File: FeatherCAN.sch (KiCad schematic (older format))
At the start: 29 parts, among them J1 Feather Long, J2 Feather Short, J3 Header, J4 PicoBlade, U1 DS3231MZ, U2 MCP2515-xST, U3 MCP2551-I-SN, U4 5V, Y1 16MHz

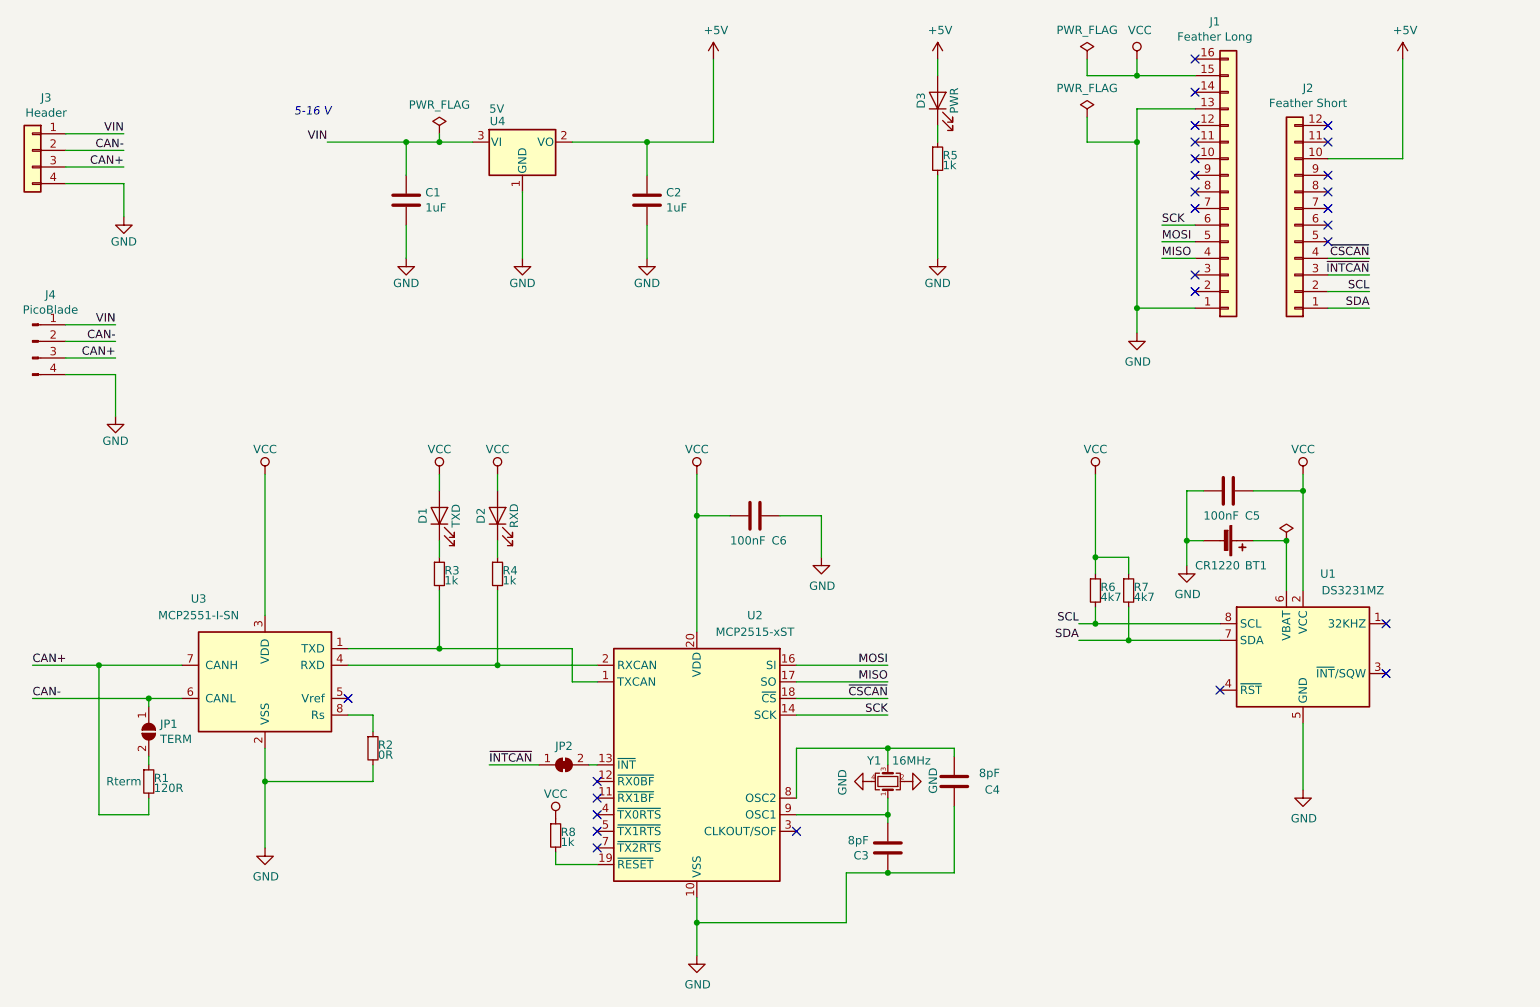
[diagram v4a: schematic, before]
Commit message: add CAN transeiver lines for STM32 Feather peripheral
STM32 Feather has CAN RX/TX on #9 and #10. Can be cut if user wants to
use pins on other Feather.
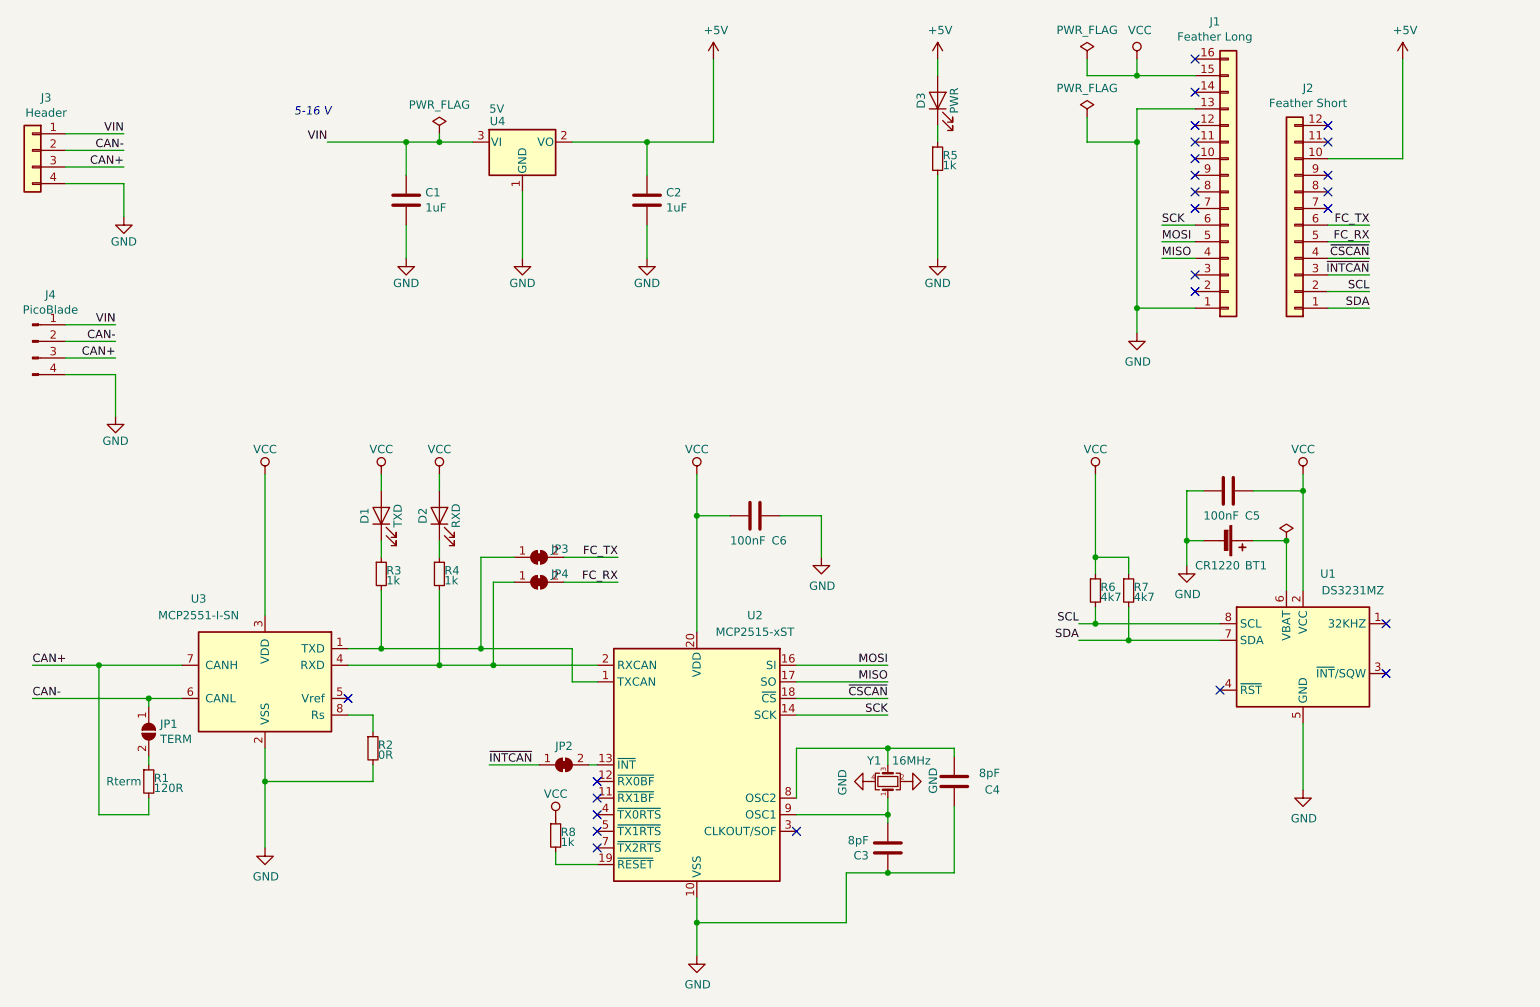
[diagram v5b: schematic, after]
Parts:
- added JP3, JP4: INT, KiCad/Jumper.pretty:SolderJumper-2_P1.3mm_Bridged_RoundedPad1.0x1.5mm, symbol Jumper:SolderJumper_2_Bridged
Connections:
- net FC_RX: now reaches J2.5 (Pin_5)
- net FC_RX: now also JP4.2 (B)
- net FC_TX: now reaches J2.6 (Pin_6)
- net FC_TX: now also JP3.2 (B)
- net at R3.2, U2.1 (TXCAN), U3.1 (TXD): now also JP3.1 (A)
- net at R4.2, U2.2 (RXCAN), U3.4 (RXD): now also JP4.1 (A)
- no-connect marks 27 -> 25
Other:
- moved on the sheet: D1, D2, R3, R4
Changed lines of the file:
@@
 L power:VCC #PWR0105
 U 1 1 5E018A7F
+P 3500 3700
+F 0 "#PWR0105" H 3500 3550 50  0001 C CNN
+F 1 "VCC" H 3500 3850 50  0000 C CNN
+F 2 "" H 3500 3700 50  0001 C CNN
+F 3 "" H 3500 3700 50  0001 C CNN
+	1    3500 3700
+	1    0    0    -1
+$EndComp
+$Comp
+L Device:R_Small R3
+U 1 1 5E018A85
+P 3500 4300
+F 0 "R3" H 3530 4320 50  0000 L CNN
+F 1 "1k" H 3530 4260 50  0000 L CNN
+F 2 "KiCad/Resistor_SMD.pretty:R_0603_1608Metric" H 3500 4300 50  0001 C CNN
+F 3 "" H 3500 4300 50  0001 C CNN
+	1    3500 4300
+	1    0    0    -1
+$EndComp
+Wire Wire Line
+	3500 3700 3500 3800
+Wire Wire Line
+	3500 4100 3500 4200
+$Comp
+L Device:LED D2
+U 1 1 5E021C73
+P 3850 3950
+F 0 "D2" H 3850 4050 50  0000 C CNN
+F 1 "RXD" H 3850 3850 50  0000 C CNN
+F 2 "KiCad/LED_SMD.pretty:LED_0603_1608Metric" H 3850 3950 50  0001 C CNN
+F 3 "http://www.kingbrightusa.com/images/catalog/SPEC/APT1608LSECK-J4-PRV.pdf" H 3850 3950 50  0001 C CNN
+F 4 "Kingbright" H 3850 3950 60  0001 C CNN "MFN"
+F 5 "APT1608LSECK/J4-PRV " H 3850 3950 60  0001 C CNN "MFP"
+F 6 "Orange 605nm LED Indication - Discrete 1.8V 2mA 0603 (1608 Metric) " H 3850 3950 60  0001 C CNN "Description"
+F 7 "Orange" H 3850 3950 50  0001 C CNN "Characteristics"
+F 8 "Digikey" H 3850 3950 50  0001 C CNN "Vendor"
+F 9 "754-1931-1-ND " H 3850 3950 50  0001 C CNN "SKU"
+	1    3850 3950
+	0    -1   -1   0
+$EndComp
+$Comp
+L power:VCC #PWR0106
+U 1 1 5E021C79
 P 3850 3700
-F 0 "#PWR0105" H 3850 3550 50  0001 C CNN
+F 0 "#PWR0106" H 3850 3550 50  0001 C CNN
 F 1 "VCC" H 3850 3850 50  0000 C CNN
 F 2 "" H 3850 3700 50  0001 C CNN
@@
 $EndComp
 $Comp
-L Device:R_Small R3
-U 1 1 5E018A85
+L Device:R_Small R4
+U 1 1 5E021C7F
 P 3850 4300
-F 0 "R3" H 3880 4320 50  0000 L CNN
+F 0 "R4" H 3880 4320 50  0000 L CNN
 F 1 "1k" H 3880 4260 50  0000 L CNN
 F 2 "KiCad/Resistor_SMD.pretty:R_0603_1608Metric" H 3850 4300 50  0001 C CNN
@@
 	3850 4100 3850 4200
 $Comp
-L Device:LED D2
-U 1 1 5E021C73
-P 4200 3950
-F 0 "D2" H 4200 4050 50  0000 C CNN
-F 1 "RXD" H 4200 3850 50  0000 C CNN
-F 2 "KiCad/LED_SMD.pretty:LED_0603_1608Metric" H 4200 3950 50  0001 C CNN
-F 3 "http://www.kingbrightusa.com/images/catalog/SPEC/APT1608LSECK-J4-PRV.pdf" H 4200 3950 50  0001 C CNN
-F 4 "Kingbright" H 4200 3950 60  0001 C CNN "MFN"
-F 5 "APT1608LSECK/J4-PRV " H 4200 3950 60  0001 C CNN "MFP"
-F 6 "Orange 605nm LED Indication - Discrete 1.8V 2mA 0603 (1608 Metric) " H 4200 3950 60  0001 C CNN "Description"
-F 7 "Orange" H 4200 3950 50  0001 C CNN "Characteristics"
-F 8 "Digikey" H 4200 3950 50  0001 C CNN "Vendor"
-F 9 "754-1931-1-ND " H 4200 3950 50  0001 C CNN "SKU"
-	1    4200 3950
-	0    -1   -1   0
-$EndComp
-$Comp
-L power:VCC #PWR0106
-U 1 1 5E021C79
-P 4200 3700
-F 0 "#PWR0106" H 4200 3550 50  0001 C CNN
-F 1 "VCC" H 4200 3850 50  0000 C CNN
-F 2 "" H 4200 3700 50  0001 C CNN
-F 3 "" H 4200 3700 50  0001 C CNN
-	1    4200 3700
-	1    0    0    -1
-$EndComp
-$Comp
-L Device:R_Small R4
-U 1 1 5E021C7F
-P 4200 4300
-F 0 "R4" H 4230 4320 50  0000 L CNN
-F 1 "1k" H 4230 4260 50  0000 L CNN
-F 2 "KiCad/Resistor_SMD.pretty:R_0603_1608Metric" H 4200 4300 50  0001 C CNN
-F 3 "" H 4200 4300 50  0001 C CNN
-	1    4200 4300
-	1    0    0    -1
-$EndComp
-Wire Wire Line
-	4200 3700 4200 3800
-Wire Wire Line
-	4200 4100 4200 4200
-$Comp
 L Device:LED D1
 U 1 1 5DFF2E6B
-P 3850 3950
-F 0 "D1" H 3850 4050 50  0000 C CNN
-F 1 "TXD" H 3850 3850 50  0000 C CNN
-F 2 "KiCad/LED_SMD.pretty:LED_0603_1608Metric" H 3850 3950 50  0001 C CNN
-F 3 "http://www.kingbrightusa.com/images/catalog/SPEC/APT1608LSECK-J4-PRV.pdf" H 3850 3950 50  0001 C CNN
-F 4 "Kingbright" H 3850 3950 60  0001 C CNN "MFN"
-F 5 "APT1608LSECK/J4-PRV " H 3850 3950 60  0001 C CNN "MFP"
-F 6 "Orange 605nm LED Indication - Discrete 1.8V 2mA 0603 (1608 Metric)" H 3850 3950 60  0001 C CNN "Description"
-F 7 "Orange" H 3850 3950 50  0001 C CNN "Characteristics"
-F 8 "754-1931-1-ND " H 3850 3950 50  0001 C CNN "SKU"
-F 9 "Digikey" H 3850 3950 50  0001 C CNN "Vendor"
-	1    3850 3950
+P 3500 3950
+F 0 "D1" H 3500 4050 50  0000 C CNN
+F 1 "TXD" H 3500 3850 50  0000 C CNN
+F 2 "KiCad/LED_SMD.pretty:LED_0603_1608Metric" H 3500 3950 50  0001 C CNN
+F 3 "http://www.kingbrightusa.com/images/catalog/SPEC/APT1608LSECK-J4-PRV.pdf" H 3500 3950 50  0001 C CNN
+F 4 "Kingbright" H 3500 3950 60  0001 C CNN "MFN"
+F 5 "APT1608LSECK/J4-PRV " H 3500 3950 60  0001 C CNN "MFP"
+F 6 "Orange 605nm LED Indication - Discrete 1.8V 2mA 0603 (1608 Metric)" H 3500 3950 60  0001 C CNN "Description"
+F 7 "Orange" H 3500 3950 50  0001 C CNN "Characteristics"
+F 8 "754-1931-1-ND " H 3500 3950 50  0001 C CNN "SKU"
+F 9 "Digikey" H 3500 3950 50  0001 C CNN "Vendor"
+	1    3500 3950
 	0    -1   -1   0
 $EndComp
@@
 NoConn ~ 9200 1600
 NoConn ~ 9200 1700
-NoConn ~ 9200 2200
-NoConn ~ 9200 2300
 NoConn ~ 8400 2500
 NoConn ~ 8400 2600
@@
 $EndComp
 Wire Wire Line
-	3850 4750 3300 4750
-Wire Wire Line
-	4650 4750 3850 4750
-Connection ~ 3850 4750
-Wire Wire Line
-	3850 4400 3850 4750
-Wire Wire Line
-	4200 4850 3300 4850
-Wire Wire Line
-	4800 4850 4200 4850
-Connection ~ 4200 4850
-Wire Wire Line
-	4200 4400 4200 4850
+	3500 4750 3300 4750
+Wire Wire Line
+	4650 4750 4100 4750
+Connection ~ 3500 4750
+Wire Wire Line
+	3500 4400 3500 4750
+Wire Wire Line
+	3850 4850 3300 4850
+Connection ~ 3850 4850
+Wire Wire Line
+	3850 4400 3850 4850
 $Comp
 L Device:C C4
@@
 	3175 1700 3650 1700
 Connection ~ 3650 1700
+Wire Wire Line
+	9200 2300 9450 2300
+Wire Wire Line
+	9200 2200 9450 2200
+Text Label 9450 2200 2    50   ~ 0
+FC_TX
+Text Label 9450 2300 2    50   ~ 0
+FC_RX
+Connection ~ 4100 4750
+Wire Wire Line
+	4100 4750 3500 4750
+Text Label 4925 4200 2    50   ~ 0
+FC_TX
+Text Label 4925 4350 2    50   ~ 0
+FC_RX
+$Comp
+L Jumper:SolderJumper_2_Bridged JP3
+U 1 1 5E2A57BA
+P 4450 4200
+F 0 "JP3" H 4575 4250 50  0000 C CNN
+F 1 "INT" H 4450 4314 50  0001 C CNN
+F 2 "KiCad/Jumper.pretty:SolderJumper-2_P1.3mm_Bridged_RoundedPad1.0x1.5mm" H 4450 4200 50  0001 C CNN
+F 3 "~" H 4450 4200 50  0001 C CNN
+F 4 "nofit" H 4450 4200 50  0001 C CNN "Config"
+F 5 "Cut to remove INT connection to Feather" H 4450 4200 50  0001 C CNN "Notes"
+	1    4450 4200
+	1    0    0    -1
+$EndComp
+$Comp
+L Jumper:SolderJumper_2_Bridged JP4
+U 1 1 5E2BEBB3
+P 4450 4350
+F 0 "JP4" H 4575 4400 50  0000 C CNN
+F 1 "INT" H 4450 4464 50  0001 C CNN
+F 2 "KiCad/Jumper.pretty:SolderJumper-2_P1.3mm_Bridged_RoundedPad1.0x1.5mm" H 4450 4350 50  0001 C CNN
+F 3 "~" H 4450 4350 50  0001 C CNN
+F 4 "nofit" H 4450 4350 50  0001 C CNN "Config"
+F 5 "Cut to remove INT connection to Feather" H 4450 4350 50  0001 C CNN "Notes"
+	1    4450 4350
+	1    0    0    -1
+$EndComp
+Wire Wire Line
+	4100 4200 4300 4200
+Wire Wire Line
+	4100 4200 4100 4750
+Wire Wire Line
+	4600 4200 4925 4200
+Wire Wire Line
+	4600 4350 4925 4350
+Wire Wire Line
+	3850 4850 4175 4850
+Wire Wire Line
+	4300 4350 4175 4350
+Wire Wire Line
+	4175 4350 4175 4850
+Connection ~ 4175 4850
+Wire Wire Line
+	4175 4850 4800 4850
 $EndSCHEMATC

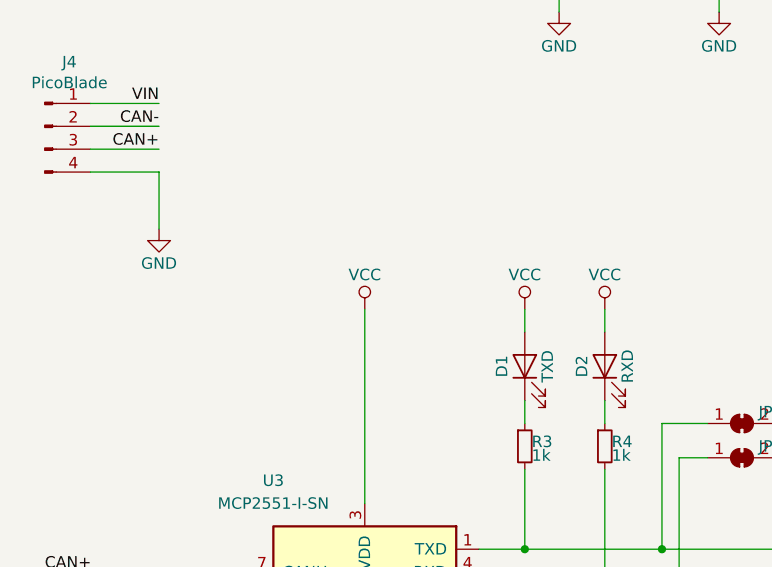
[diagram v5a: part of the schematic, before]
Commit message: MCP2515 Vdd is +5 V
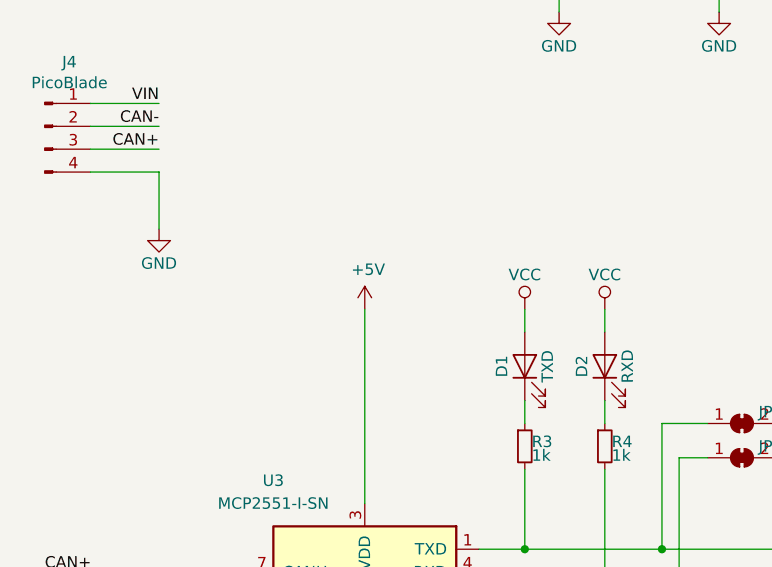
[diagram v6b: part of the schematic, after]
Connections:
- net +5V: now also U3.3 (VDD)
- net VCC: no longer U3.3 (VDD)
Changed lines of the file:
@@
 Sheet 1 1
 Title "FeatherCAN"
-Date "2019-12-23"
-Rev "1.0"
+Date "2020-01-22"
+Rev "1.1"
 Comp "JBR Engineering Research Ltd"
 Comment1 "J. Whittington 2019"
@@
 F 1 "MCP2515-xST" H 5050 6250 50  0000 C CNN
 F 2 "KiCad/Package_SO.pretty:TSSOP-20_4.4x6.5mm_P0.65mm" H 5400 4550 50  0001 C CIN
-F 3 "http://ww1.microchip.com/downloads/en/DeviceDoc/21801e.pdf" H 5500 4650 50  0001 C CNN
+F 3 "http://ww1.microchip.com/downloads/en/DeviceDoc/MCP2515-Stand-Alone-CAN-Controller-with-SPI-20001801J.pdf" H 5500 4650 50  0001 C CNN
 F 4 "Microchip Technology" H 5400 5450 50  0001 C CNN "MFN"
 F 5 "MCP2515T-I/ST" H 5400 5450 50  0001 C CNN "MFP"
@@
 	5400 3700 5400 3950
 $Comp
-L power:VCC #PWR0110
-U 1 1 5E02BB71
-P 2800 3700
-F 0 "#PWR0110" H 2800 3550 50  0001 C CNN
-F 1 "VCC" H 2800 3850 50  0000 C CNN
-F 2 "" H 2800 3700 50  0001 C CNN
-F 3 "" H 2800 3700 50  0001 C CNN
-	1    2800 3700
-	1    0    0    -1
-$EndComp
-$Comp
 L power:GND #PWR0111
 U 1 1 5E02DE0F
@@
 Wire Wire Line
 	4175 4850 4800 4850
+$Comp
+L power:+5V #PWR0110
+U 1 1 5E2A847B
+P 2800 3700
+F 0 "#PWR0110" H 2800 3550 50  0001 C CNN
+F 1 "+5V" H 2815 3873 50  0000 C CNN
+F 2 "" H 2800 3700 50  0001 C CNN
+F 3 "" H 2800 3700 50  0001 C CNN
+	1    2800 3700
+	1    0    0    -1
+$EndComp
 $EndSCHEMATC
